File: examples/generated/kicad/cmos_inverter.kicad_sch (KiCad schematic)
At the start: 4 parts

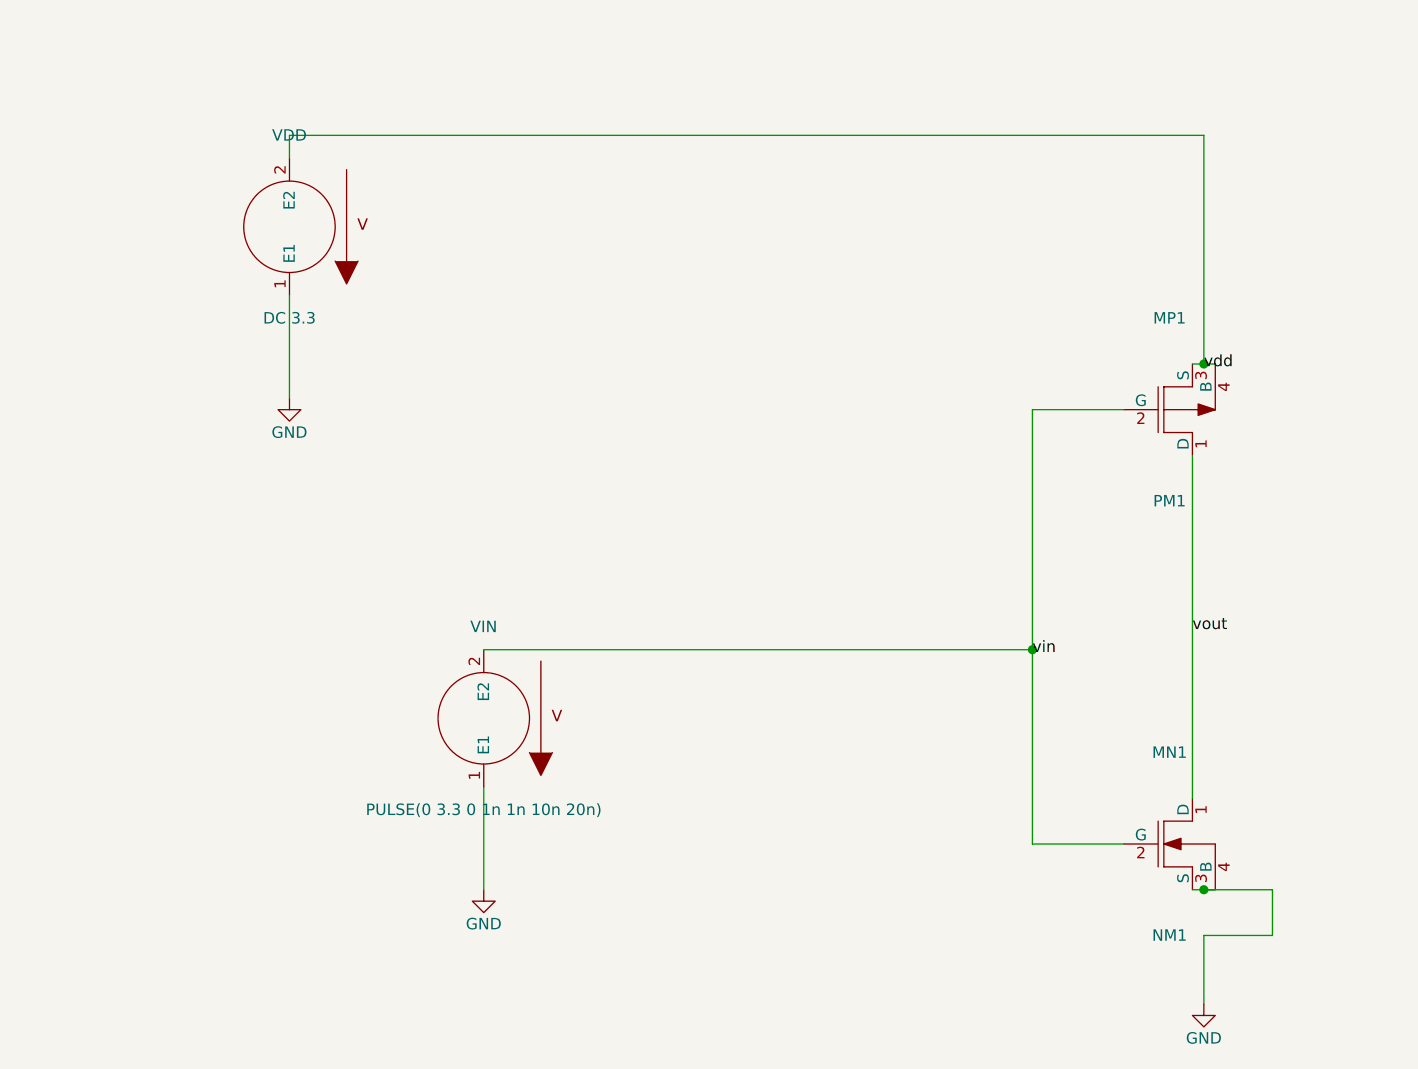
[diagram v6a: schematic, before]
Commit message: Attempt to fix wire kinking (where example showed in cmos inverter).
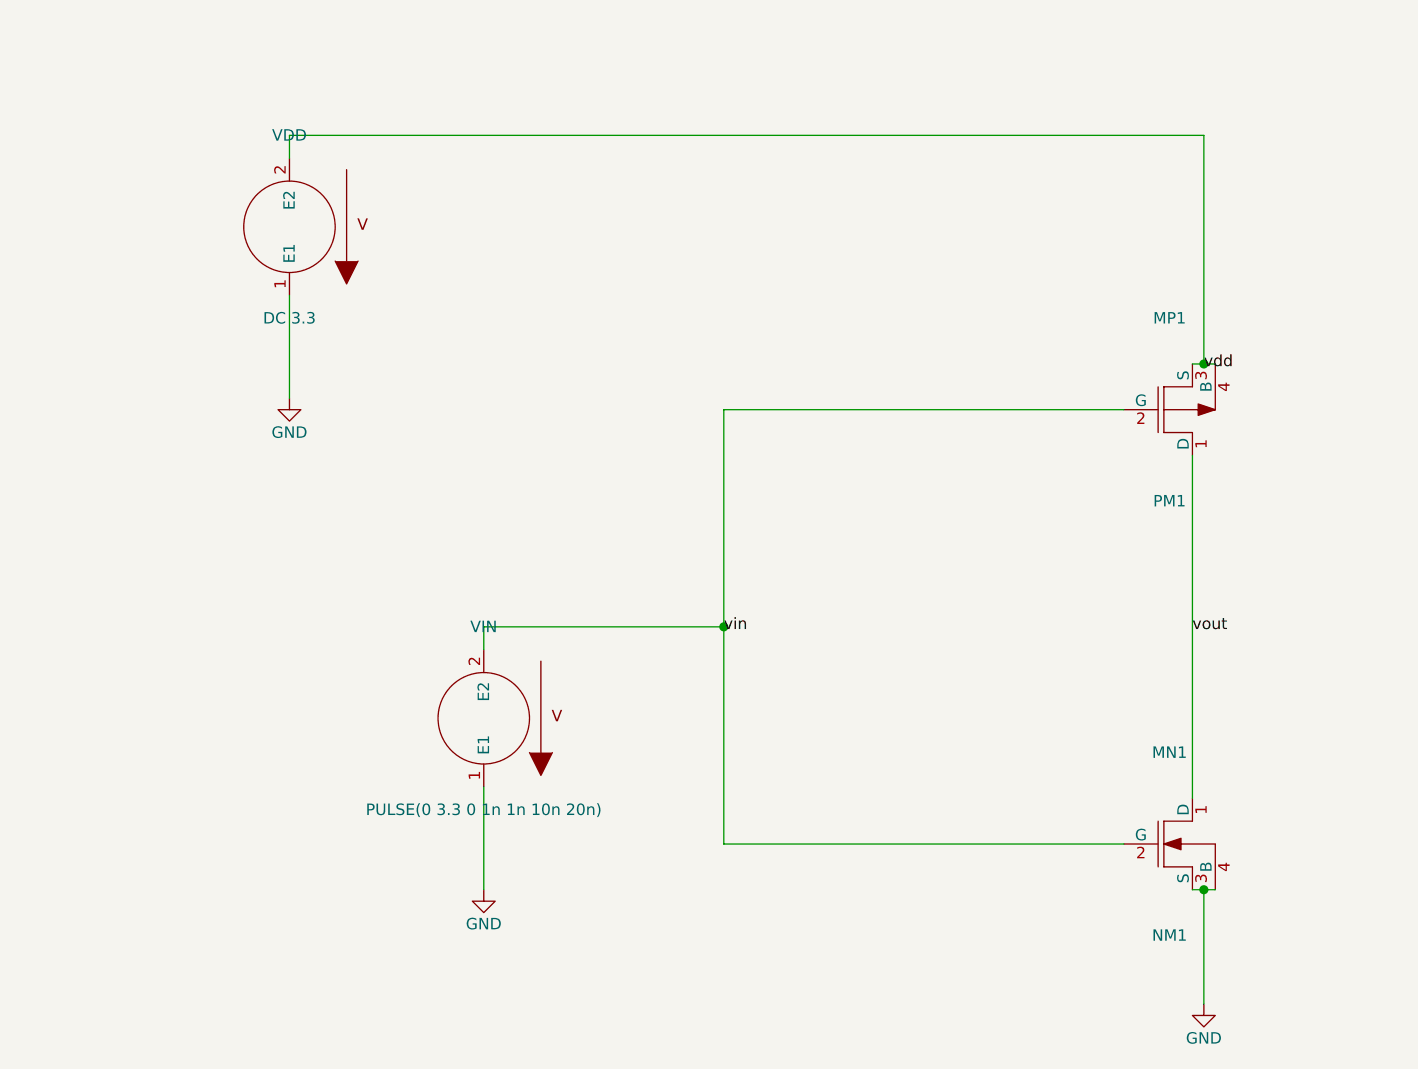
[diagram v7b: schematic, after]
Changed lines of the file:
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@@
     )
   )
-  (label "vin" (at 144.78 115.57 0)
+  (label "vin" (at 110.49 113.03 0)
     (effects (font (size 1.27 1.27)))
   )
@@
     (stroke (width 0) (type solid) (color 0 0 0 0))
   )
-  (wire (pts (xy 144.78 88.90) (xy 144.78 137.16))
+  (wire (pts (xy 83.82 115.57) (xy 83.82 113.03))
     (stroke (width 0) (type solid) (color 0 0 0 0))
   )
-  (wire (pts (xy 83.82 115.57) (xy 144.78 115.57))
+  (wire (pts (xy 83.82 113.03) (xy 110.49 113.03))
     (stroke (width 0) (type solid) (color 0 0 0 0))
   )
-  (wire (pts (xy 154.94 88.90) (xy 144.78 88.90))
+  (wire (pts (xy 154.94 88.90) (xy 110.49 88.90))
     (stroke (width 0) (type solid) (color 0 0 0 0))
   )
-  (wire (pts (xy 154.94 137.16) (xy 144.78 137.16))
+  (wire (pts (xy 110.49 88.90) (xy 110.49 113.03))
+    (stroke (width 0) (type solid) (color 0 0 0 0))
+  )
+  (wire (pts (xy 154.94 137.16) (xy 110.49 137.16))
+    (stroke (width 0) (type solid) (color 0 0 0 0))
+  )
+  (wire (pts (xy 110.49 137.16) (xy 110.49 113.03))
     (stroke (width 0) (type solid) (color 0 0 0 0))
   )
@@
     (stroke (width 0) (type solid) (color 0 0 0 0))
   )
-  (wire (pts (xy 163.83 154.94) (xy 163.83 147.32))
+  (wire (pts (xy 163.83 154.94) (xy 163.83 142.24))
     (stroke (width 0) (type solid) (color 0 0 0 0))
   )
-  (wire (pts (xy 163.83 147.32) (xy 171.45 147.32))
-    (stroke (width 0) (type solid) (color 0 0 0 0))
-  )
-  (wire (pts (xy 171.45 147.32) (xy 171.45 142.24))
-    (stroke (width 0) (type solid) (color 0 0 0 0))
-  )
-  (wire (pts (xy 171.45 142.24) (xy 163.83 142.24))
-    (stroke (width 0) (type solid) (color 0 0 0 0))
-  )
-  (junction (at 144.78 115.57) (diameter 1.016) (color 0 0 0 0))
+  (junction (at 110.49 113.03) (diameter 1.016) (color 0 0 0 0))
   (junction (at 163.83 83.82) (diameter 1.016) (color 0 0 0 0))
   (junction (at 163.83 142.24) (diameter 1.016) (color 0 0 0 0))

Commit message: Attempt to add the right connections for the schmitt trigger. Messed up cmos inverter.
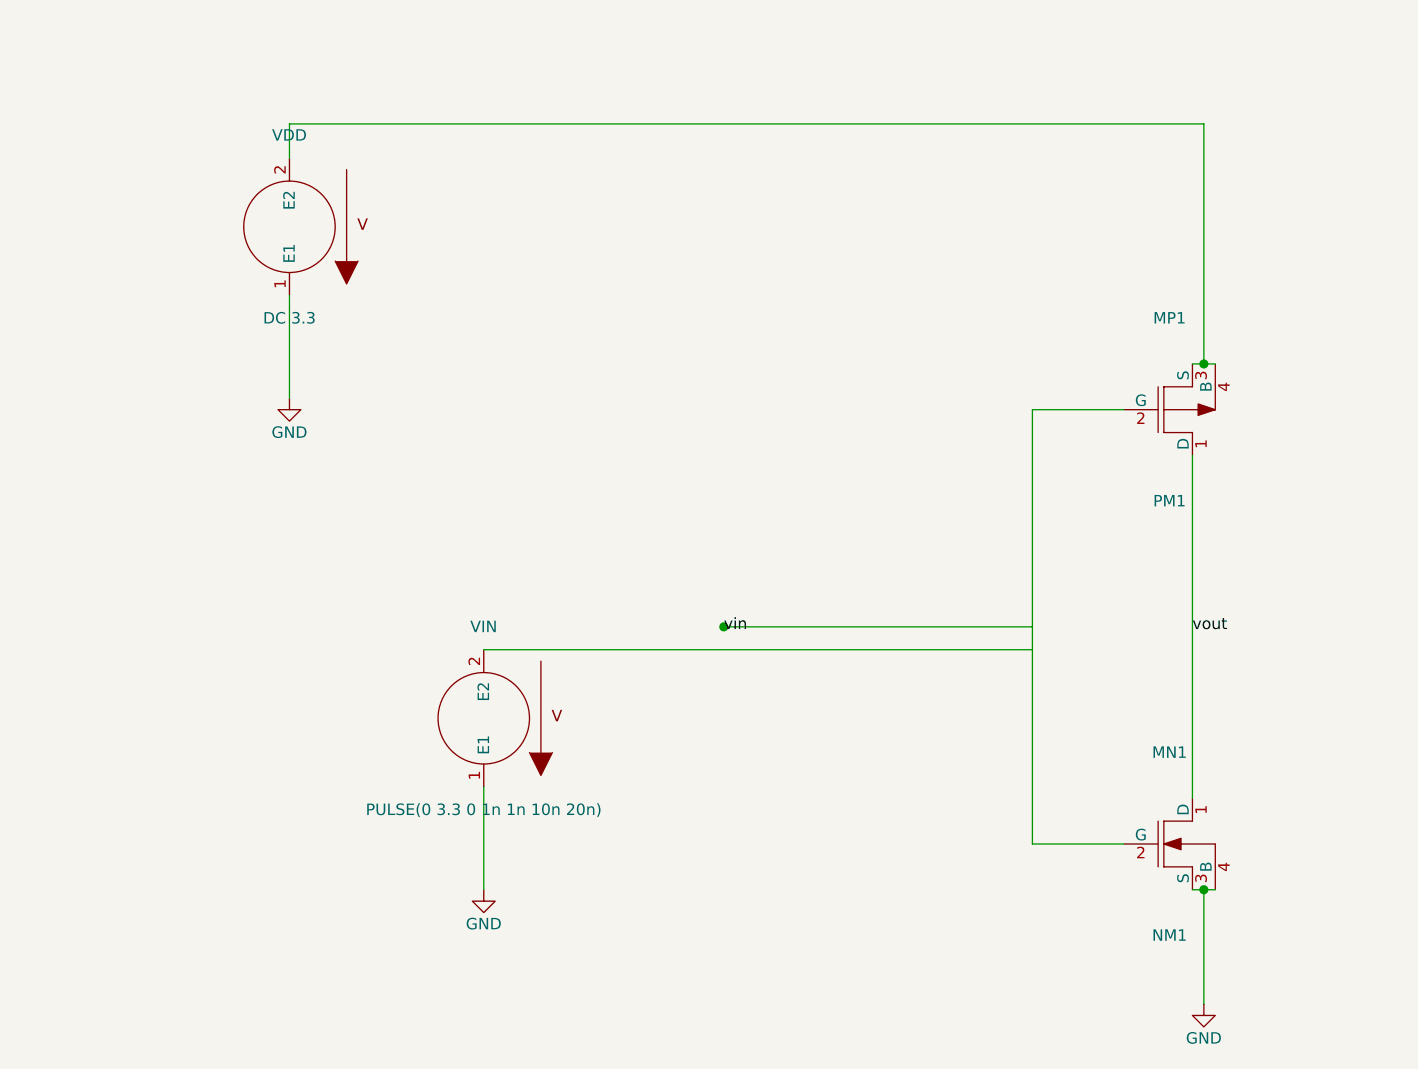
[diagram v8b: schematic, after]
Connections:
- net vin: no longer MN1.2 (G), MP1.2 (G), VIN.2 (E2)
- net vdd: no longer names the net of MP1.3 (S), MP1.4 (B), VDD.2 (E2)
- new net: MN1.2 (G), MP1.2 (G)
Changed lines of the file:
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@@
   (title_block
     (title "cmos_inverter")
-    (date "2026-03-13")
+    (date "2026-03-14")
     (comment 1 "Generated by mixedsig2cad")
   )
@@
     (effects (font (size 1.27 1.27)))
   )
-  (label "vdd" (at 163.83 83.82 0)
-    (effects (font (size 1.27 1.27)))
-  )
   (label "vout" (at 162.56 113.03 0)
     (effects (font (size 1.27 1.27)))
@@
     (stroke (width 0) (type solid) (color 0 0 0 0))
   )
-  (wire (pts (xy 83.82 115.57) (xy 83.82 113.03))
+  (wire (pts (xy 144.78 88.90) (xy 144.78 137.16))
     (stroke (width 0) (type solid) (color 0 0 0 0))
   )
-  (wire (pts (xy 83.82 113.03) (xy 110.49 113.03))
+  (wire (pts (xy 144.78 113.03) (xy 110.49 113.03))
     (stroke (width 0) (type solid) (color 0 0 0 0))
   )
-  (wire (pts (xy 154.94 88.90) (xy 110.49 88.90))
+  (wire (pts (xy 83.82 115.57) (xy 144.78 115.57))
     (stroke (width 0) (type solid) (color 0 0 0 0))
   )
-  (wire (pts (xy 110.49 88.90) (xy 110.49 113.03))
+  (wire (pts (xy 154.94 88.90) (xy 144.78 88.90))
     (stroke (width 0) (type solid) (color 0 0 0 0))
   )
-  (wire (pts (xy 154.94 137.16) (xy 110.49 137.16))
+  (wire (pts (xy 154.94 137.16) (xy 144.78 137.16))
     (stroke (width 0) (type solid) (color 0 0 0 0))
   )
-  (wire (pts (xy 110.49 137.16) (xy 110.49 113.03))
+  (wire (pts (xy 62.23 60.96) (xy 62.23 57.15))
     (stroke (width 0) (type solid) (color 0 0 0 0))
   )
-  (wire (pts (xy 62.23 60.96) (xy 62.23 58.42))
+  (wire (pts (xy 62.23 57.15) (xy 163.83 57.15))
     (stroke (width 0) (type solid) (color 0 0 0 0))
   )
-  (wire (pts (xy 62.23 58.42) (xy 163.83 58.42))
+  (wire (pts (xy 163.83 57.15) (xy 163.83 83.82))
     (stroke (width 0) (type solid) (color 0 0 0 0))
   )
-  (wire (pts (xy 163.83 58.42) (xy 163.83 83.82))
-    (stroke (width 0) (type solid) (color 0 0 0 0))
-  )
